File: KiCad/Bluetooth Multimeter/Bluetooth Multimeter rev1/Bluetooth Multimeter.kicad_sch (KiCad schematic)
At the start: 30 parts, among them J1 V/Ohm, J2 Com, J3 mA, J4 A, J5 Parallel Prot, K1 Low Range, K2 Medium Range, K3 High Range, K4 UH Range (Ohm Only), K5 V/Ohm Switch, U1 ItsyBitsy_NRF52840_Big

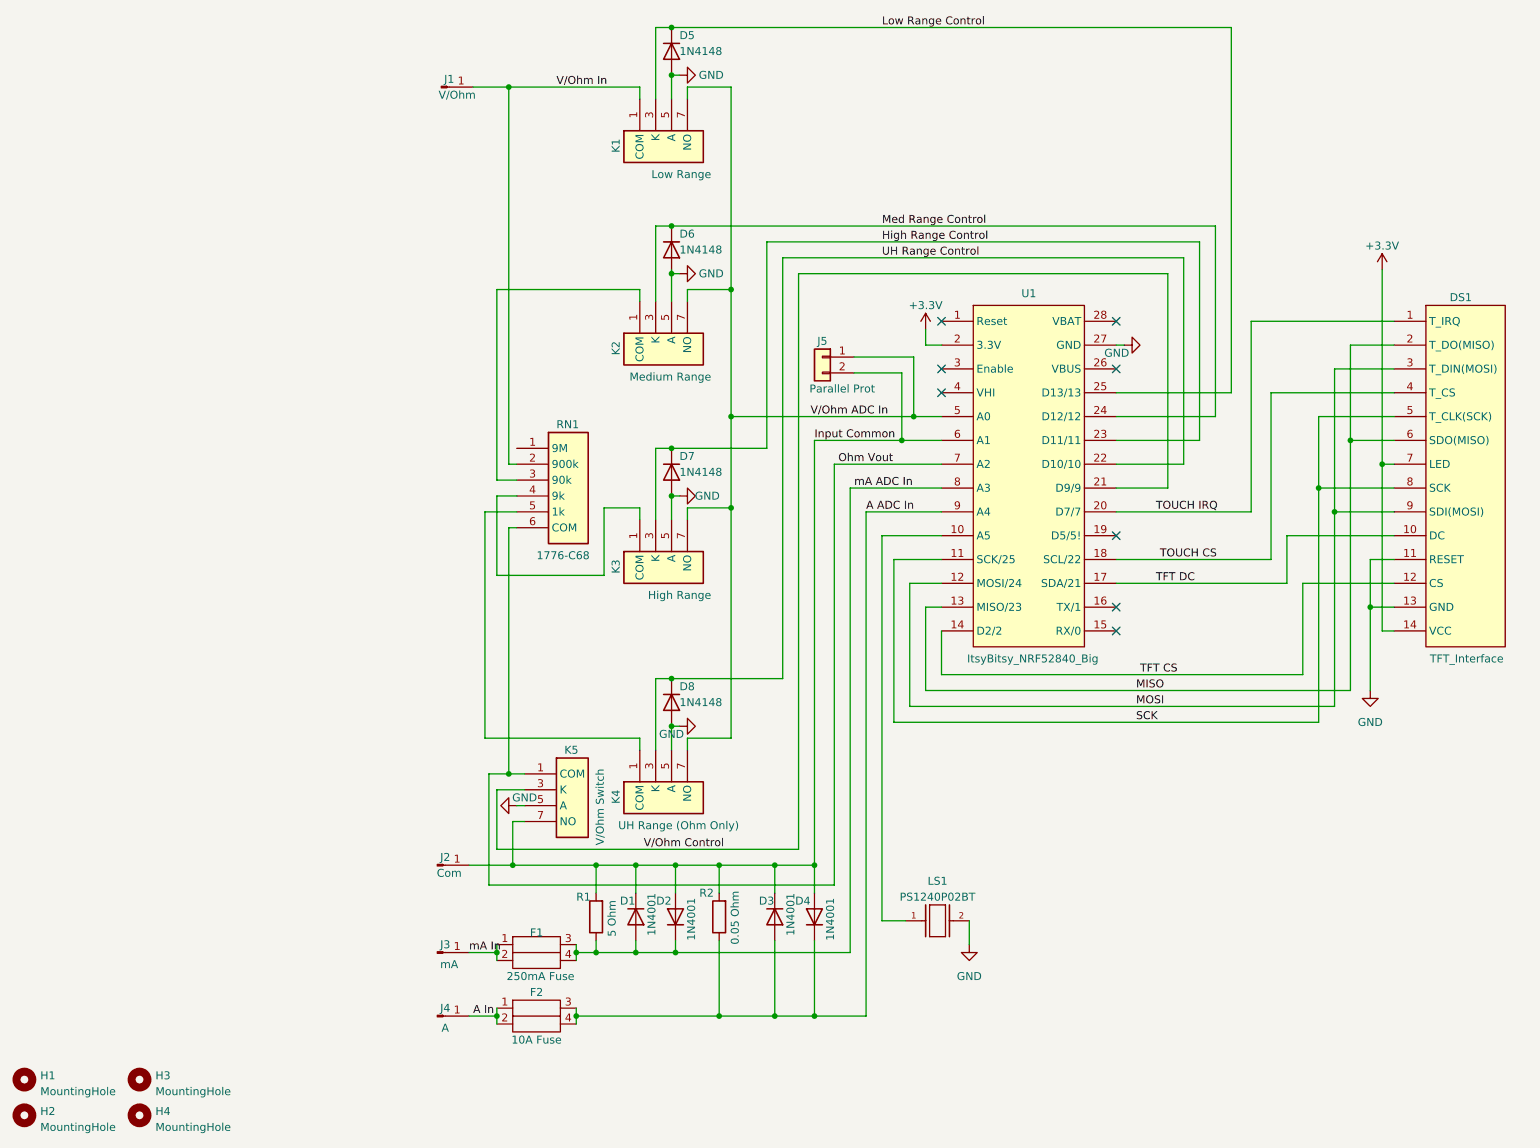
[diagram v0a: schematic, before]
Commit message: Reformatted footprints & Routed PCB rev 2
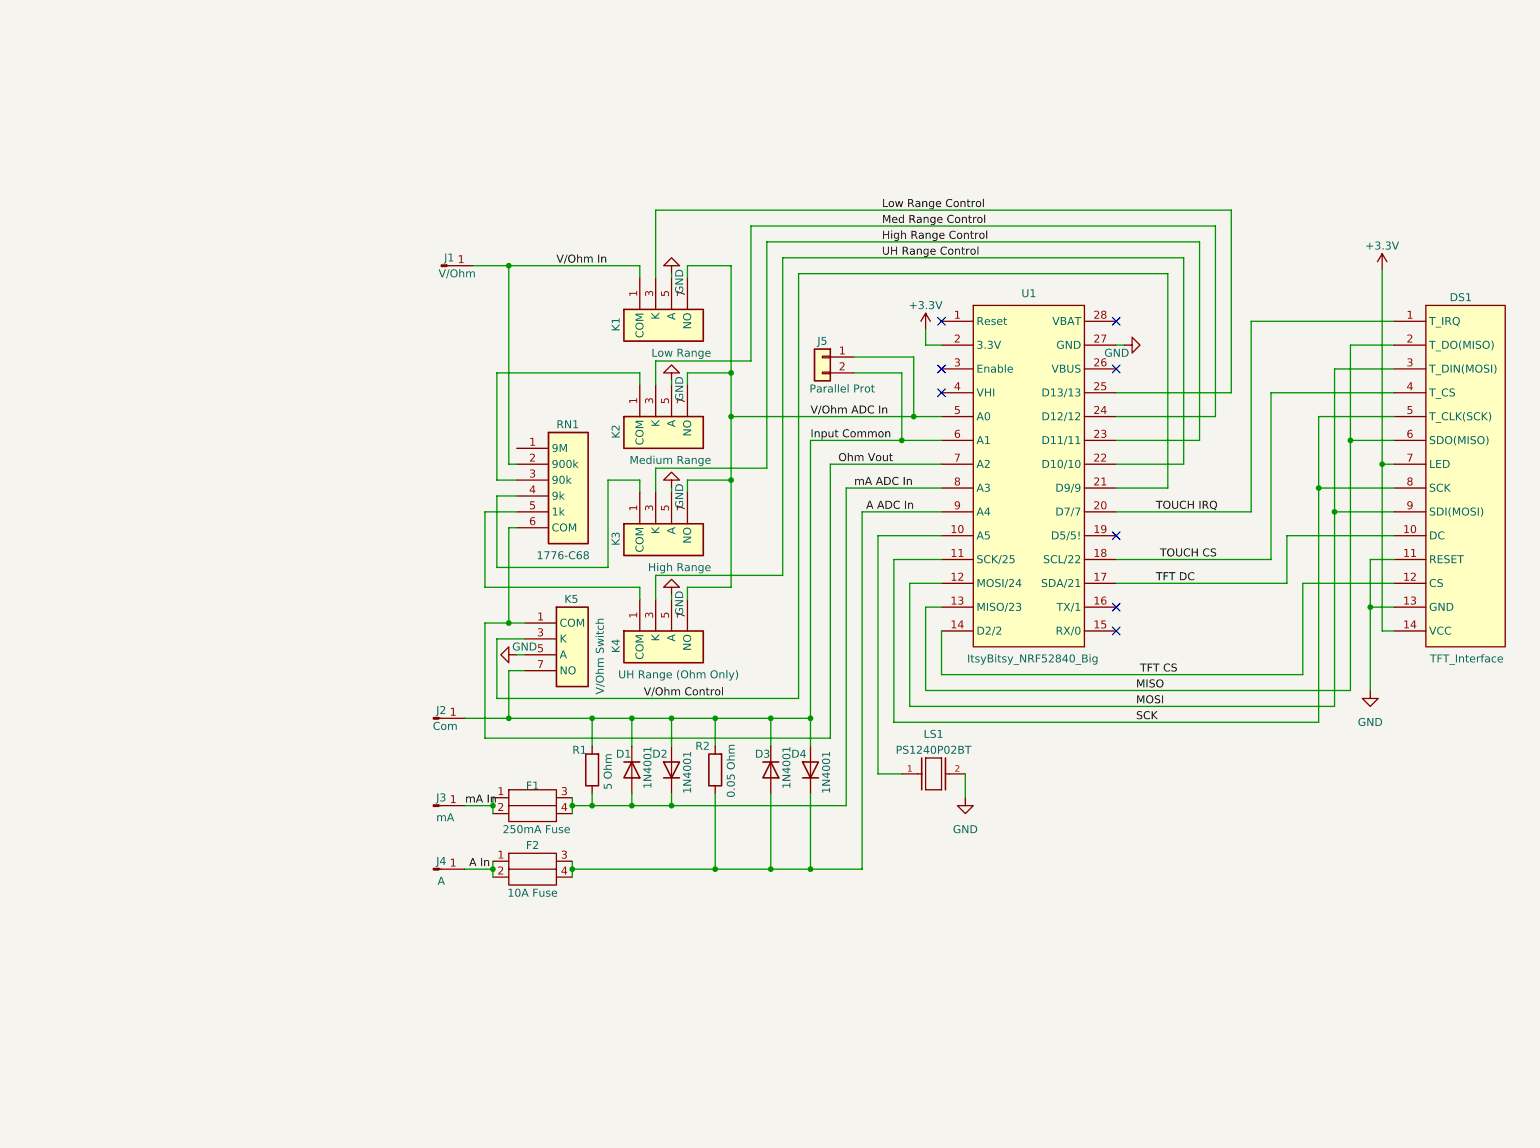
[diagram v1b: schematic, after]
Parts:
- removed D5, D6, D7, D8: 1N4148, Diode_THT:D_DO-35_SOD27_P7.62mm_Horizontal, symbol Diode:1N4148
- removed H1, H2, H3, H4: MountingHole, 502ProjectFootprints:MountingHole_3mm, symbol Mechanical:MountingHole
- F1: footprint 502ProjectFootprints:LF124061_2 -> 502ProjectFootprints:250mA Fuse rev2
- F2: footprint 502ProjectFootprints:LF124041_3 -> 502ProjectFootprints:10A Fuse Oval rev2
- K1, K2, K3, K4, K5: footprint 502ProjectFootprints:SIL03-1A72-71_4 -> 502ProjectFootprints:SIL03-1A72-71DrevB
- R2: footprint 502ProjectFootprints:LOB-1528272_3 -> 502ProjectFootprints:0.05 Ohm 5W Resistor rev2
- RN1: footprint 502ProjectFootprints:1776-C68-1 -> 502ProjectFootprints:1776C68
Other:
- moved on the sheet: D1, D2, D3, D4, F1, F2, J1, J2, J3, J4, K1, K2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
